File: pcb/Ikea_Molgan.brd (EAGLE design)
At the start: 28 x 35 mm, 22 parts, among them U2 MEGA328P-AU

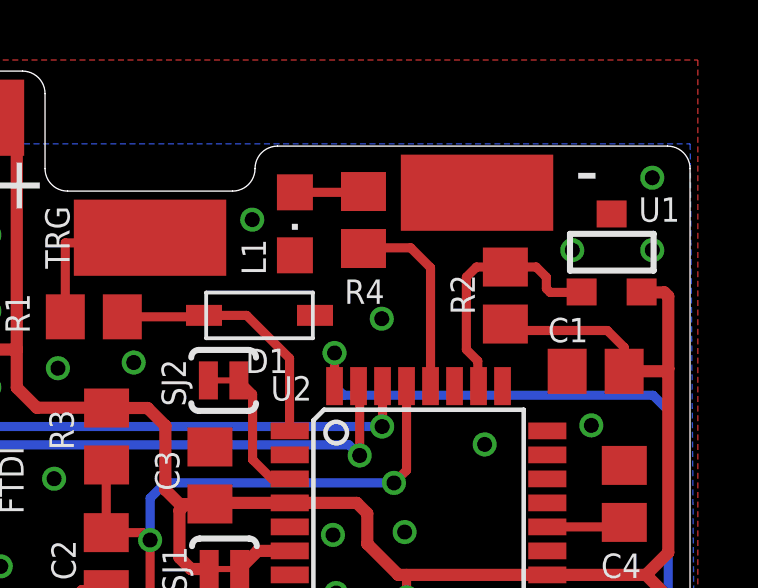
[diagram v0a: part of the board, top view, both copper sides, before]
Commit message: Temperatursensor hinzugefügt und LED entfernt
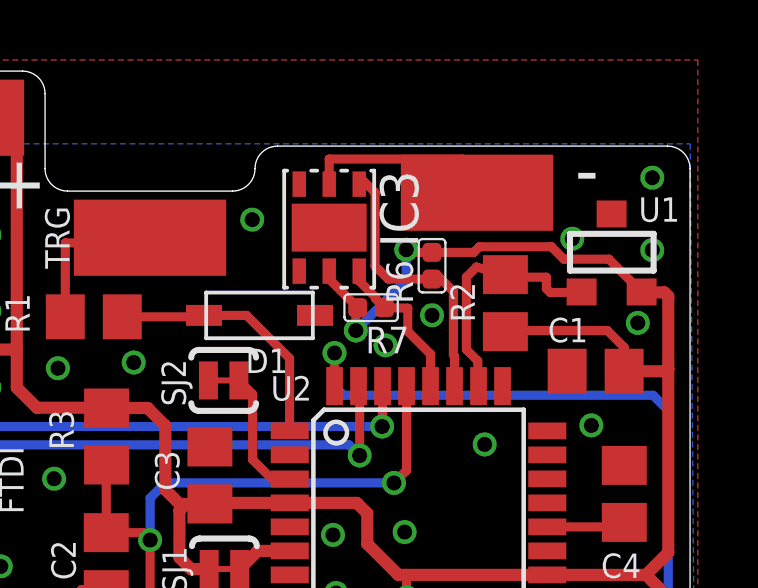
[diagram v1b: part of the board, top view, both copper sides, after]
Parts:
- removed L1: (no value), adafruit:CHIPLED_0805
- removed R4: 56, rcl:R0805
- added IC3: SI7021, Sensor:DFN6
- added R6, R7: 4k7, Discrete:R0402
- moved R2 0.25 mm to (35.8, 31.3)
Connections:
- removed net N$2: L1.A, R4.1
- removed net N$3: R4.2, U2.28
- new net SCL: IC3.6, R7.1, U2.28
- new net SDA: IC3.1, R6.1, U2.27
- net GND: now also IC3.2; no longer L1.C
- net VCC: now also IC3.5, R6.2, R7.2
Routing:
- net VCC: track 92.9 -> 107.3 mm, vias 2 -> 4
- net SDA: track 0.00 -> 9.64 mm
- net GND: track 0.00 -> 6.89 mm, vias 22 -> 24
- net N$3: track 6.47 -> 0.00 mm
- net SCL: track 0.00 -> 5.26 mm
- net N$2: track 2.30 -> 0.00 mm
